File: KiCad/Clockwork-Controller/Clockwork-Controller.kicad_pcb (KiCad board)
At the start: 2 copper layers, 56.4 x 94.2 mm, 97 parts, among them CN2 PJ-307N5, J2 to DIN-6 Male, J3 Pause Button, J4 ICSP, J5 LED-Connector, Q1 AO3400A, Q2 SS8050, Q3 SS8050, Q4 SS8050, SW1 Guide/Follow, SW2 Mode -, SW3 Mode +, SW4 Frame -, SW5 Frame +, U1 ECS-TXO-3225MV-160-TR, U2 AP2210N-3.3TRG1, U3 74HCT14, U4 G3VM-61VY3(TR), U5 MCP4725, U6 LMC6482, U7 ATmega328P-A

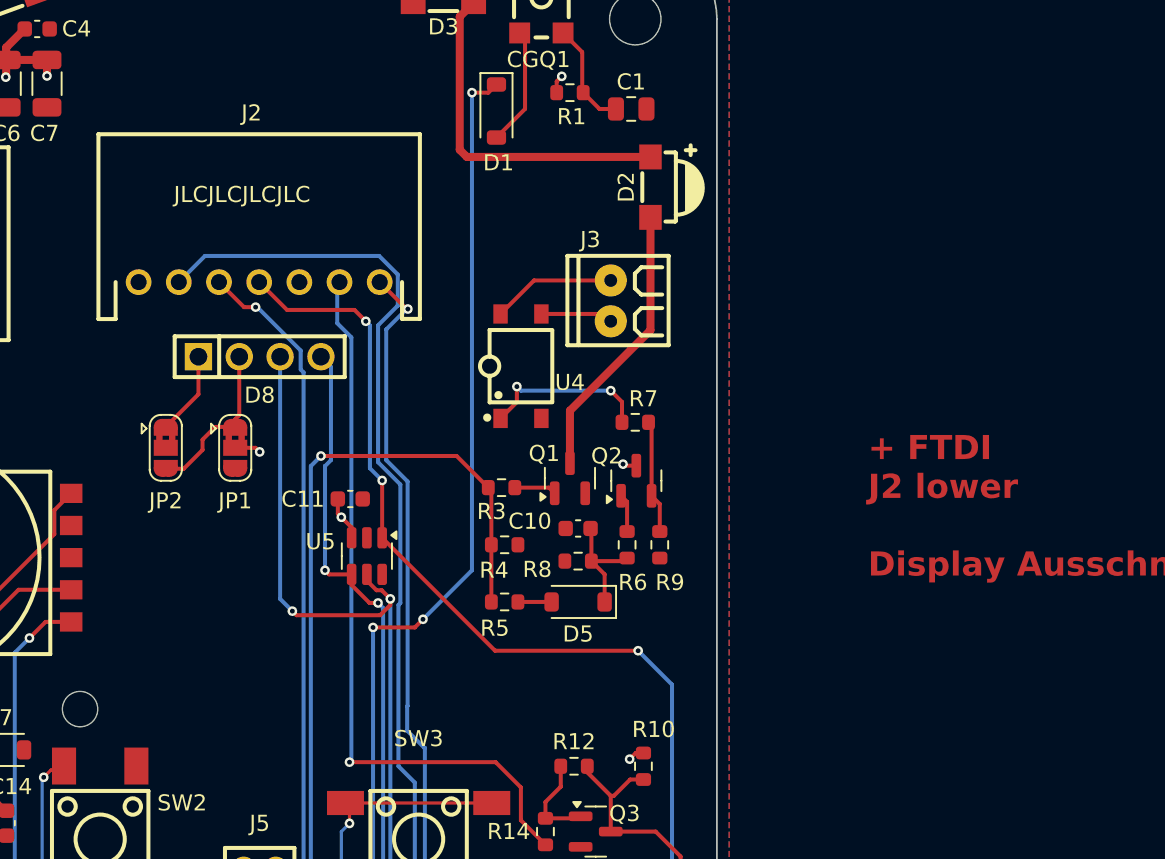
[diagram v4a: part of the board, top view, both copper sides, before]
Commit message: Lowered J2 further towards the display to allow better cable securing
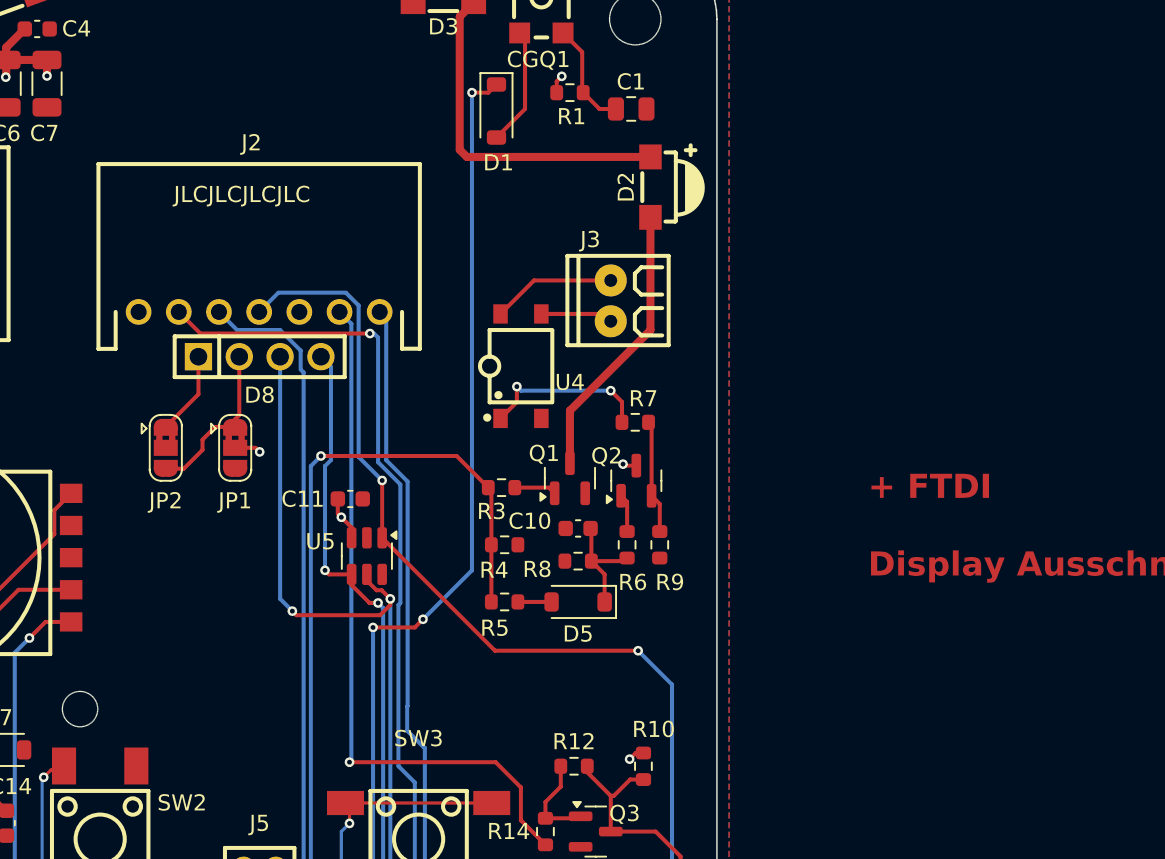
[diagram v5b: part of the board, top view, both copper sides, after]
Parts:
- moved J2 1.86 mm to (66.5, 43.6)
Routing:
- net /DAC_EN: track 82.5 -> 76.4 mm, vias 2 -> 3
- net /Stop_EN: track 59.3 -> 56.2 mm, vias 2 -> 1
- net /M-Pin: track 45.9 -> 43.9 mm
- net /Proj_ID: track 73.5 -> 72.7 mm, vias 2 -> 1
- net /Ctrl_V: track 59.6 -> 60.1 mm, vias 3 -> 2
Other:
- board text added: "+ FTDI Display Ausschnitt 1mm tiefer"
- board text removed: "+ FTDI J2 lower Display Ausschnitt 1mm tiefer"
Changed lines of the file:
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@@
 	(footprint "easyEDA:CONN-TH_S7B-XH-A-LF-SN"
 		(layer "F.Cu")
-		(at 66.5155 41.7585)
+		(at 66.5155 43.6145)
 		(property "Reference" "J2"
 			(at -0.4755 -10.5165 0)
@@
 		(layer "Edge.Cuts")
 	)
-	(gr_text "+ FTDI\nJ2 lower\n\nDisplay Ausschnitt 1mm tiefer"
+	(gr_text "+ FTDI\n\nDisplay Ausschnitt 1mm tiefer"
 		(at 104.394 60.198 0)
 		(layer "F.Cu")
@@
 	)
 	(segment
-		(start 71.374 44.317884)
-		(end 71.374 41.9)
-		(width 0.25)
-		(layer "B.Cu")
-		(net 10)
-	)
-	(segment
-		(start 72.253 45.196884)
-		(end 71.374 44.317884)
-		(width 0.25)
-		(layer "B.Cu")
-		(net 10)
-	)
-	(segment
-		(start 71.374 41.9)
-		(end 71.5155 41.7585)
+		(start 72.253 71.511)
+		(end 72.253 44.352)
 		(width 0.25)
 		(layer "B.Cu")
@@
 	)
 	(segment
-		(start 72.253 71.511)
-		(end 72.253 45.196884)
+		(start 72.253 44.352)
+		(end 71.5155 43.6145)
 		(width 0.25)
 		(layer "B.Cu")
@@
 	)
 	(segment
+		(start 73.406 44.958)
+		(end 62.859 44.958)
+		(width 0.25)
+		(layer "F.Cu")
+		(net 29)
+	)
+	(segment
 		(start 75.946 80.772)
 		(end 68.056 80.772)
@@
 	)
 	(segment
+		(start 62.859 44.958)
+		(end 61.5155 43.6145)
+		(width 0.25)
+		(layer "F.Cu")
+		(net 29)
+	)
+	(segment
 		(start 76.2 96.774)
 		(end 75.732 97.242)
@@
 	)
 	(via
-		(at 76.2 96.774)
+		(at 73.406 44.958)
 		(size 0.6)
 		(drill 0.3)
@@
 		(net 29)
 	)
-	(segment
-		(start 75.184 71.882)
-		(end 75.184 61.843884)
-		(width 0.25)
-		(layer "B.Cu")
-		(net 29)
-	)
-	(segment
-		(start 73.914 44.45)
-		(end 75.1405 43.2235)
-		(width 0.25)
-		(layer "B.Cu")
-		(net 29)
-	)
-	(segment
-		(start 75.184 61.843884)
-		(end 75.301 61.726884)
-		(width 0.25)
-		(layer "B.Cu")
+	(via
+		(at 76.2 96.774)
+		(size 0.6)
+		(drill 0.3)
+		(layers "F.Cu" "B.Cu")
 		(net 29)
 	)
 	(segment
-		(start 75.301 61.726884)
-		(end 75.301 54.351116)
+		(start 76.2 72.898)
+		(end 75.184 71.882)
 		(width 0.25)
 		(layer "B.Cu")
@@
 	)
 	(segment
-		(start 63.142 40.132)
-		(end 61.5155 41.7585)
+		(start 76.2 80.518)
+		(end 76.2 72.898)
 		(width 0.25)
 		(layer "B.Cu")
@@
 	)
 	(segment
-		(start 75.1405 41.292509)
-		(end 73.979991 40.132)
+		(start 75.184 71.882)
+		(end 75.184 61.843884)
 		(width 0.25)
 		(layer "B.Cu")
@@
 	)
 	(segment
-		(start 75.301 54.351116)
-		(end 73.914 52.964116)
+		(start 73.914 52.964116)
+		(end 73.914 45.212)
 		(width 0.25)
 		(layer "B.Cu")
@@
 	)
 	(segment
-		(start 73.979991 40.132)
-		(end 63.142 40.132)
+		(start 75.301 61.726884)
+		(end 75.301 54.351116)
 		(width 0.25)
 		(layer "B.Cu")
@@
 	)
 	(segment
-		(start 76.2 80.518)
-		(end 76.2 72.898)
+		(start 73.66 44.958)
+		(end 73.406 44.958)
 		(width 0.25)
 		(layer "B.Cu")
@@
 	)
 	(segment
-		(start 76.2 72.898)
-		(end 75.184 71.882)
+		(start 73.914 45.212)
+		(end 73.66 44.958)
 		(width 0.25)
 		(layer "B.Cu")
@@
 	)
 	(segment
-		(start 73.914 52.964116)
-		(end 73.914 44.45)
+		(start 75.184 61.843884)
+		(end 75.301 61.726884)
 		(width 0.25)
 		(layer "B.Cu")
@@
 	)
 	(segment
-		(start 75.1405 43.2235)
-		(end 75.1405 41.292509)
+		(start 75.301 54.351116)
+		(end 73.914 52.964116)
 		(width 0.25)
 		(layer "B.Cu")
@@
 	)
 	(segment
-		(start 75.691 43.434)
-		(end 74.0155 41.7585)
-		(width 0.25)
-		(layer "F.Cu")
-		(net 30)
-	)
-	(segment
 		(start 77.47 95.895)
 		(end 76.825 95.25)
@@
 	)
 	(segment
-		(start 75.7655 43.434)
-		(end 75.691 43.434)
-		(width 0.25)
-		(layer "F.Cu")
-		(net 30)
-	)
-	(segment
 		(start 77.332 96.15)
 		(end 77.47 96.012)
@@
 	)
 	(via
-		(at 75.7655 43.434)
-		(size 0.6)
-		(drill 0.3)
-		(layers "F.Cu" "B.Cu")
-		(net 30)
-	)
-	(via
 		(at 76.825 95.25)
 		(size 0.6)
@@
 	)
 	(segment
-		(start 75.751 68.12806)
-		(end 75.751 54.16472)
-		(width 0.25)
-		(layer "B.Cu")
-		(net 30)
-	)
-	(segment
-		(start 75.723 68.15606)
-		(end 75.751 68.12806)
+		(start 74.422 52.83572)
+		(end 74.422 44.021)
 		(width 0.25)
 		(layer "B.Cu")
@@
 	)
 	(segment
-		(start 75.692 43.434)
-		(end 75.7655 43.434)
+		(start 76.79206 70.737)
+		(end 75.723 69.66794)
 		(width 0.25)
 		(layer "B.Cu")
@@
 	)
 	(segment
-		(start 74.422 52.83572)
-		(end 74.422 44.704)
+		(start 75.723 68.15606)
+		(end 75.751 68.12806)
 		(width 0.25)
 		(layer "B.Cu")
@@
 	)
 	(segment
-		(start 74.422 44.704)
-		(end 75.692 43.434)
+		(start 76.825 70.737)
+		(end 76.79206 70.737)
 		(width 0.25)
 		(layer "B.Cu")
@@
 	)
 	(segment
-		(start 75.723 69.66794)
-		(end 75.723 68.15606)
+		(start 76.825 95.25)
+		(end 76.825 70.737)
 		(width 0.25)
 		(layer "B.Cu")
@@
 	)
 	(segment
-		(start 75.751 54.16472)
-		(end 74.422 52.83572)
+		(start 75.751 68.12806)
+		(end 75.751 54.16472)
 		(width 0.25)
 		(layer "B.Cu")
@@
 	)
 	(segment
-		(start 76.825 70.737)
-		(end 76.79206 70.737)
+		(start 74.422 44.021)
+		(end 74.0155 43.6145)
 		(width 0.25)
 		(layer "B.Cu")
@@
 	)
 	(segment
-		(start 76.79206 70.737)
-		(end 75.723 69.66794)
+		(start 75.751 54.16472)
+		(end 74.422 52.83572)
 		(width 0.25)
 		(layer "B.Cu")
@@
 	)
 	(segment
-		(start 76.825 95.25)
-		(end 76.825 70.737)
+		(start 75.723 69.66794)
+		(end 75.723 68.15606)
 		(width 0.25)
 		(layer "B.Cu")
@@
 	)
 	(segment
-		(start 72.448 43.492)
-		(end 68.249 43.492)
-		(width 0.25)
-		(layer "F.Cu")
-		(net 31)
-	)
-	(segment
-		(start 68.249 43.492)
-		(end 66.5155 41.7585)
-		(width 0.25)
-		(layer "F.Cu")
-		(net 31)
-	)
-	(segment
 		(start 74.168 57.669)
 		(end 81.1928 64.6938)
@@
 		(net 31)
 	)
-	(segment
-		(start 73.152 44.196)
-		(end 72.448 43.492)
-		(width 0.25)
-		(layer "F.Cu")
-		(net 31)
-	)
 	(via
 		(at 74.168 54.102)
@@
 		(net 31)
 	)
-	(via
-		(at 73.152 44.196)
-		(size 0.6)
-		(drill 0.3)
-		(layers "F.Cu" "B.Cu")
+	(segment
+		(start 67.712 42.418)
+		(end 66.5155 43.6145)
+		(width 0.25)
+		(layer "B.Cu")
 		(net 31)
 	)
 	(segment
-		(start 73.406 44.45)
-		(end 73.152 44.196)
+		(start 71.909991 42.418)
+		(end 67.712 42.418)
 		(width 0.25)
 		(layer "B.Cu")
@@
 	)
 	(segment
+		(start 72.703 43.211009)
+		(end 71.909991 42.418)
+		(width 0.25)
+		(layer "B.Cu")
+		(net 31)
+	)
+	(segment
 		(start 92.202 80.5688)
 		(end 90.4494 82.3214)
@@
 	)
 	(segment
-		(start 73.406 53.34)
-		(end 73.406 44.45)
+		(start 72.703 52.637)
+		(end 72.703 43.211009)
 		(width 0.25)
 		(layer "B.Cu")
@@
 	(segment
 		(start 74.168 54.102)
-		(end 73.406 53.34)
+		(end 72.703 52.637)
 		(width 0.25)
 		(layer "B.Cu")
@@
 	)
 	(segment
-		(start 65.574 43.317)
-		(end 64.0155 41.7585)
-		(width 0.25)
-		(layer "F.Cu")
-		(net 34)
-	)
-	(segment
 		(start 69.761 104.559)
 		(end 69.596 104.394)
@@
 	)
 	(segment
-		(start 66.294 43.317)
-		(end 65.574 43.317)
-		(width 0.25)
-		(layer "F.Cu")
-		(net 34)
-	)
-	(segment
 		(start 69.733 105.998)
 		(end 69.733 104.531)
@@
 		(net 34)
 	)
-	(via
-		(at 66.294 43.317)
-		(size 0.6)
-		(drill 0.3)
-		(layers "F.Cu" "B.Cu")
-		(net 34)
-	)
 	(segment
 		(start 69.279 104.077)
@@
 	)
 	(segment
-		(start 66.396701 43.317)
-		(end 66.294 43.317)
+		(start 69.279 47.379)
+		(end 69.279 104.077)
 		(width 0.25)
 		(layer "B.Cu")
@@
 	)
 	(segment
-		(start 69.1 47.2)
-		(end 69.279 47.379)
+		(start 64.0155 43.6145)
+		(end 65.1405 44.7395)
 		(width 0.25)
 		(layer "B.Cu")
@@
 	)
 	(segment
-		(start 69.279 47.379)
-		(end 69.279 104.077)
+		(start 67.819201 44.7395)
+		(end 69.1 46.020299)
+		(width 0.25)
+		(layer "B.Cu")
+		(net 34)
+	)
+	(segment
+		(start 65.1405 44.7395)
+		(end 67.819201 44.7395)
 		(width 0.25)
 		(layer "B.Cu")
@@
 	(segment
 		(start 69.1 46.020299)
-		(end 66.396701 43.317)
+		(end 69.1 47.2)
 		(width 0.25)
 		(layer "B.Cu")
@@
 	(segment
 		(start 69.1 47.2)
-		(end 69.1 46.020299)
+		(end 69.279 47.379)
 		(width 0.25)
 		(layer "B.Cu")

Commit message: Enlarging wirestrap holes (4mm)
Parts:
- H1: footprint Peacemans Teile:Kabelbinder 3mm -> Peacemans Teile:Kabelbinder 4mm
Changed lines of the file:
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@@
 		)
 	)
-	(footprint "Peacemans Teile:Kabelbinder 3mm"
+	(footprint "Peacemans Teile:Kabelbinder 4mm"
 		(layer "F.Cu")
 		(at 66.4802 25.3492)
@@
 			)
 		)
-		(property "Footprint" "Peacemans Teile:Kabelbinder 3mm"
+		(property "Footprint" "Peacemans Teile:Kabelbinder 4mm"
 			(at 0 0 0)
 			(unlocked yes)
@@
 		)
 		(pad "" np_thru_hole oval
-			(at -3.8 0)
-			(size 1.5 3)
-			(drill oval 1.5 3)
+			(at -4.2 0)
+			(size 1.5 4.2)
+			(drill oval 1.5 4.2)
 			(layers "*.Mask")
 		)
 		(pad "" np_thru_hole oval
-			(at 3.7 0)
-			(size 1.5 3)
-			(drill oval 1.5 3)
+			(at 4.1 0)
+			(size 1.5 4.2)
+			(drill oval 1.5 4.2)
 			(layers "*.Mask")
 		)
